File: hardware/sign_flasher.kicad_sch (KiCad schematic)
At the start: 39 parts, among them Q1 TBD, Q2 TBD, U1 NE555D, U2 NE555D

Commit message: finished design and layout with TODOs
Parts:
- added D12, D16, D20, D24, D4, D8: LED, LED_THT:LED_D5.0mm, symbol Device:LED
- added J1: Battery, Connector_JST:JST_XH_B2B-XH-A_1x02_P2.50mm_Vertical, symbol Connector:Conn_01x02_Socket
- C1: renamed from C3; value 10nF -> 10n; footprint (none) -> Capacitor_THT:CP_Radial_D4.0mm_P2.00mm
- C2: renamed from C5; value 2.2uF -> 2.2u; footprint (none) -> Capacitor_THT:CP_Radial_D4.0mm_P2.00mm; symbol Device:C -> Device:C_Polarized
- C3: renamed from C4; value 10nF -> 10n; footprint (none) -> Capacitor_THT:CP_Radial_D4.0mm_P2.00mm
- C4: renamed from C6; value 2.2uF -> 2.2u; footprint (none) -> Capacitor_THT:CP_Radial_D4.0mm_P2.00mm; symbol Device:C -> Device:C_Polarized
- C5: renamed from C1; value 220uF -> 220u
- D1, D2, D3: footprint (none) -> LED_THT:LED_D5.0mm
- D10: renamed from D8; footprint (none) -> LED_THT:LED_D5.0mm
- D11: renamed from D9; footprint (none) -> LED_THT:LED_D5.0mm
- D13: renamed from D10; footprint (none) -> LED_THT:LED_D5.0mm
- D14: renamed from D11; footprint (none) -> LED_THT:LED_D5.0mm
- D15: renamed from D12; footprint (none) -> LED_THT:LED_D5.0mm
- D17: renamed from D13; footprint (none) -> LED_THT:LED_D5.0mm
- D18: renamed from D14; footprint (none) -> LED_THT:LED_D5.0mm
- D19: renamed from D15; footprint (none) -> LED_THT:LED_D5.0mm
- D21: renamed from D16; footprint (none) -> LED_THT:LED_D5.0mm
- D22: renamed from D17; footprint (none) -> LED_THT:LED_D5.0mm
- D23: renamed from D18; footprint (none) -> LED_THT:LED_D5.0mm
- D5: renamed from D4; footprint (none) -> LED_THT:LED_D5.0mm
- D6: renamed from D5; footprint (none) -> LED_THT:LED_D5.0mm
- D7: renamed from D6; footprint (none) -> LED_THT:LED_D5.0mm
- D9: renamed from D7; footprint (none) -> LED_THT:LED_D5.0mm
- Q1: value TBD -> BC557; footprint (none) -> Package_TO_SOT_THT:TO-92; symbol Device:Q_PNP_BCE -> Device:Q_PNP_CBE
- Q2: value TBD -> BC547; footprint (none) -> Package_TO_SOT_THT:TO-92; symbol Device:Q_NPN_EBC -> Device:Q_NPN_CBE
- R1, R2, R3, R4, R7, R8: footprint (none) -> Resistor_THT:R_Axial_DIN0207_L6.3mm_D2.5mm_P7.62mm_Horizontal
- R5: renamed from R6; footprint (none) -> Resistor_THT:R_Axial_DIN0207_L6.3mm_D2.5mm_P7.62mm_Horizontal
- R6: renamed from R5; footprint (none) -> Resistor_THT:R_Axial_DIN0207_L6.3mm_D2.5mm_P7.62mm_Horizontal
- RV1: renamed from RV3; footprint (none) -> sign_flasher:TRIM_3306F-1-103
- RV2: renamed from RV1; footprint (none) -> sign_flasher:TRIM_3306F-1-103
- RV3: renamed from RV5; footprint (none) -> sign_flasher:TRIM_3306F-1-103
- RV4: footprint (none) -> sign_flasher:TRIM_3306F-1-103
- U1, U2: footprint Package_SO:SOIC-8_3.9x4.9mm_P1.27mm -> Package_DIP:DIP-8_W7.62mm
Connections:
- net 9V0: now also J1.1 (Pin_1)
- net GND: now also Q2.3 (E), D12.1 (K), D4.1 (K), D8.1 (K), J1.2 (Pin_2); no longer D11.1 (K), D3.1 (K), D7.1 (K), Q2.1 (E)
- net at R1.2: now also Q1.2 (B); no longer Q1.1 (B)
- net at R2.1, R3.1, R4.1: now also Q1.1 (C); no longer Q1.2 (C)
- new net: D7.1 (K), D8.2 (A)
- new net: D3.1 (K), D4.2 (A)
- new net: D16.1 (K), D20.1 (K), D24.1 (K), Q2.1 (C)
- new net: D23.1 (K), D24.2 (A)
- new net: D15.1 (K), D16.2 (A)
- new net: D19.1 (K), D20.2 (A)
- new net: D11.1 (K), D12.2 (A)
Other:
- moved on the sheet: Q2, R5

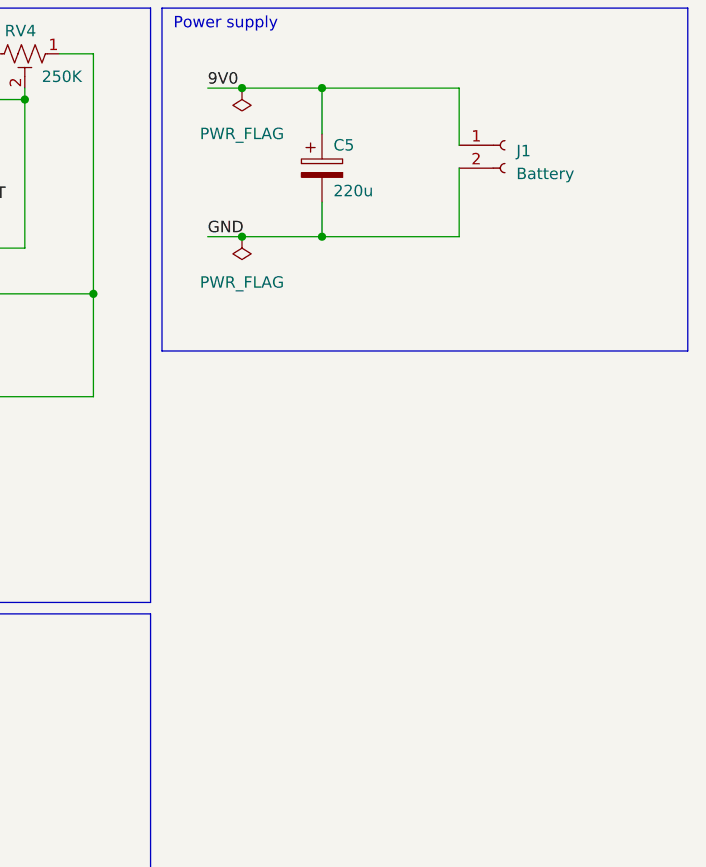
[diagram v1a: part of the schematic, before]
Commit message: get under 100mmsq, add mounting holes
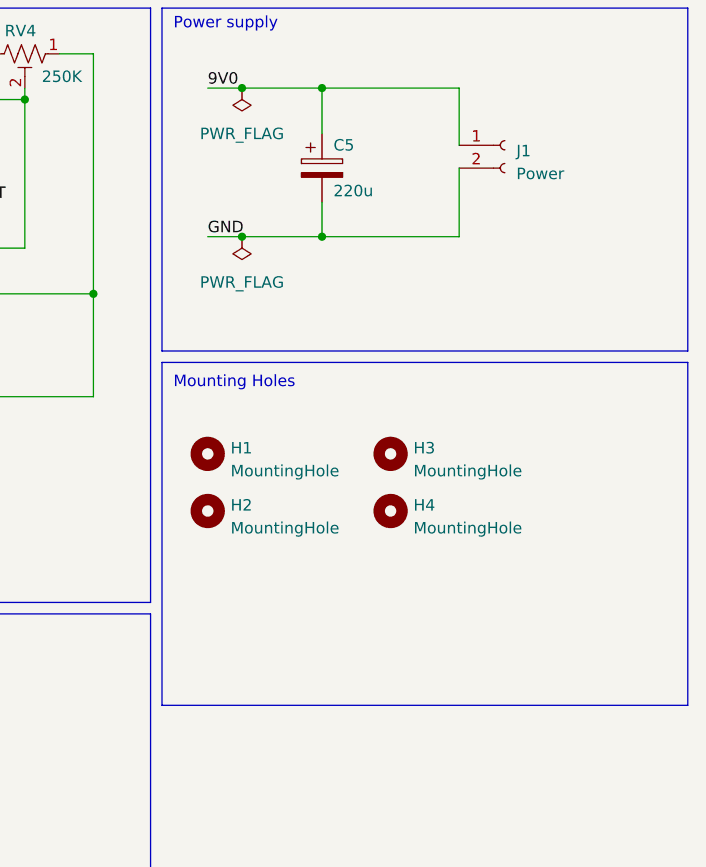
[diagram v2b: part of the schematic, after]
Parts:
- added H1, H2, H3, H4: MountingHole, MountingHole:MountingHole_4mm_Pad, symbol Mechanical:MountingHole
- J1: value Battery -> Power
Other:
- note added: "Mounting Holes"
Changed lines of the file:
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@@
+    (fill (type none))
+  )
+  (rectangle (start 144.78 52.07) (end 203.2 90.17)
+    (stroke (width 0) (type default))
     (fill (type none))
   )
@@
     (effects (font (size 1.27 1.27)) (justify left bottom))
   )
+  (text "Mounting Holes\n\n" (at 146.05 57.15 0)
+    (effects (font (size 1.27 1.27)) (justify left bottom))
+  )
   (text "Timing\n" (at 13.97 16.51 0)
     (effects (font (size 1.27 1.27)) (justify left bottom))
@@
         (path "/1d207b3d-09a4-4c99-885a-dd10de47bf46"
           (reference "#PWR04") (unit 1)
+        )
+      )
+    )
+  )
+  (symbol (lib_id "Mechanical:MountingHole") (at 170.18 62.23 0) (unit 1)
+    (in_bom yes) (on_board yes) (dnp no) (fields_autoplaced)
+    (property "Reference" "H3" (at 172.72 61.595 0)
+      (effects (font (size 1.27 1.27)) (justify left))
+    )
+    (property "Value" "MountingHole" (at 172.72 64.135 0)
+      (effects (font (size 1.27 1.27)) (justify left))
+    )
+    (property "Footprint" "MountingHole:MountingHole_4mm_Pad" (at 170.18 62.23 0)
+      (effects (font (size 1.27 1.27)) hide)
+    )
+    (property "Datasheet" "~" (at 170.18 62.23 0)
+      (effects (font (size 1.27 1.27)) hide)
+    )
+    (instances
+      (project "sign_flasher"
+        (path "/1d207b3d-09a4-4c99-885a-dd10de47bf46"
+          (reference "H3") (unit 1)
+        )
+      )
+    )
+  )
+  (symbol (lib_id "Mechanical:MountingHole") (at 149.86 62.23 0) (unit 1)
+    (in_bom yes) (on_board yes) (dnp no) (fields_autoplaced)
+    (property "Reference" "H1" (at 152.4 61.595 0)
+      (effects (font (size 1.27 1.27)) (justify left))
+    )
+    (property "Value" "MountingHole" (at 152.4 64.135 0)
+      (effects (font (size 1.27 1.27)) (justify left))
+    )
+    (property "Footprint" "MountingHole:MountingHole_4mm_Pad" (at 149.86 62.23 0)
+      (effects (font (size 1.27 1.27)) hide)
+    )
+    (property "Datasheet" "~" (at 149.86 62.23 0)
+      (effects (font (size 1.27 1.27)) hide)
+    )
+    (instances
+      (project "sign_flasher"
+        (path "/1d207b3d-09a4-4c99-885a-dd10de47bf46"
+          (reference "H1") (unit 1)
         )
       )
@@
     )
   )
+  (symbol (lib_id "Mechanical:MountingHole") (at 149.86 68.58 0) (unit 1)
+    (in_bom yes) (on_board yes) (dnp no) (fields_autoplaced)
+    (property "Reference" "H2" (at 152.4 67.945 0)
+      (effects (font (size 1.27 1.27)) (justify left))
+    )
+    (property "Value" "MountingHole" (at 152.4 70.485 0)
+      (effects (font (size 1.27 1.27)) (justify left))
+    )
+    (property "Footprint" "MountingHole:MountingHole_4mm_Pad" (at 149.86 68.58 0)
+      (effects (font (size 1.27 1.27)) hide)
+    )
+    (property "Datasheet" "~" (at 149.86 68.58 0)
+      (effects (font (size 1.27 1.27)) hide)
+    )
+    (instances
+      (project "sign_flasher"
+        (path "/1d207b3d-09a4-4c99-885a-dd10de47bf46"
+          (reference "H2") (unit 1)
+        )
+      )
+    )
+  )
   (symbol (lib_id "Timer:NE555D") (at 44.45 39.37 0) (unit 1)
     (in_bom yes) (on_board yes) (dnp no) (fields_autoplaced)
@@
     )
   )
+  (symbol (lib_id "Mechanical:MountingHole") (at 170.18 68.58 0) (unit 1)
+    (in_bom yes) (on_board yes) (dnp no) (fields_autoplaced)
+    (property "Reference" "H4" (at 172.72 67.945 0)
+      (effects (font (size 1.27 1.27)) (justify left))
+    )
+    (property "Value" "MountingHole" (at 172.72 70.485 0)
+      (effects (font (size 1.27 1.27)) (justify left))
+    )
+    (property "Footprint" "MountingHole:MountingHole_4mm_Pad" (at 170.18 68.58 0)
+      (effects (font (size 1.27 1.27)) hide)
+    )
+    (property "Datasheet" "~" (at 170.18 68.58 0)
+      (effects (font (size 1.27 1.27)) hide)
+    )
+    (instances
+      (project "sign_flasher"
+        (path "/1d207b3d-09a4-4c99-885a-dd10de47bf46"
+          (reference "H4") (unit 1)
+        )
+      )
+    )
+  )
   (symbol (lib_id "power:GND") (at 24.13 50.8 0) (unit 1)
     (in_bom yes) (on_board yes) (dnp no) (fields_autoplaced)
@@
       (effects (font (size 1.27 1.27)) (justify left))
     )
-    (property "Value" "Battery" (at 184.15 31.115 0)
-      (effects (font (size 1.27 1.27)) (justify left))
-    )
+    (property "Value" "Power" (at 184.15 31.115 0)
+      (effects (font (size 1.27 1.27)) (justify left))
+    )

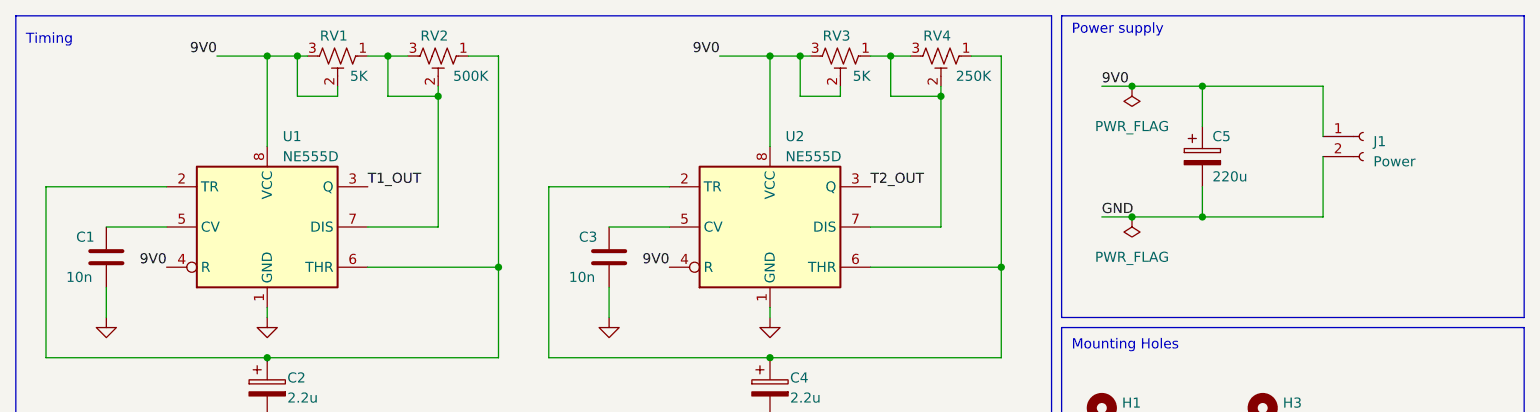
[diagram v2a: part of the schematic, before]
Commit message: Address issues identified with rev v0.01:
 - Revise schematic to indicate the need for 12V power
 - Add reverse voltage protection diode
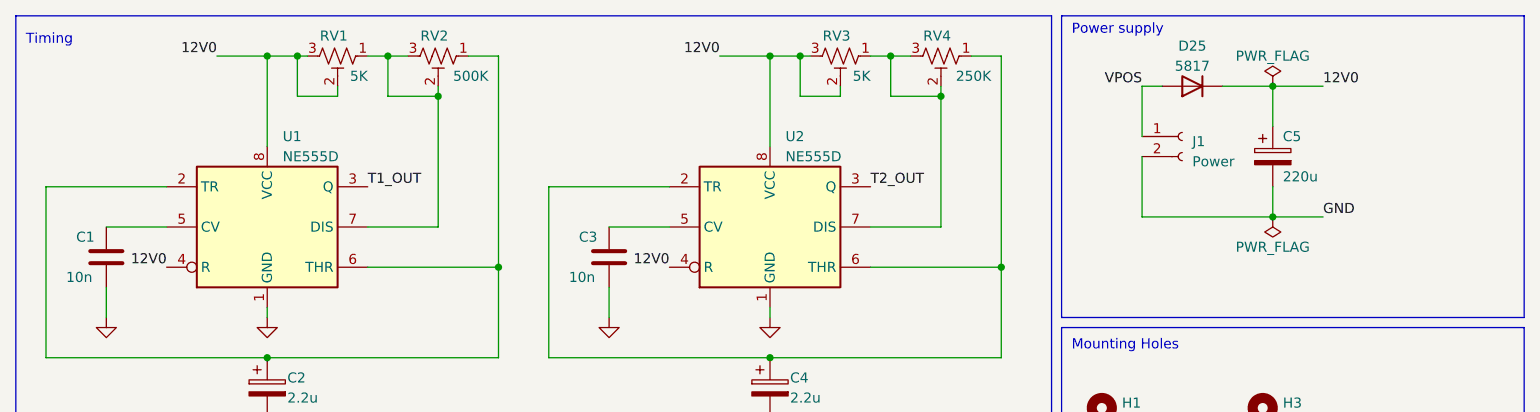
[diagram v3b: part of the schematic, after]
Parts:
- added D25: 5817, Diode_THT:D_DO-41_SOD81_P7.62mm_Horizontal, symbol Device:D
- C1, C3: footprint Capacitor_THT:CP_Radial_D4.0mm_P2.00mm -> Capacitor_THT:C_Rect_L7.2mm_W2.5mm_P5.00mm_FKS2_FKP2_MKS2_MKP2
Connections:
- net 9V0 renamed 12V0
- net 12V0: now also D25.1 (K); no longer J1.1 (Pin_1)
- new net VPOS: D25.2 (A), J1.1 (Pin_1)
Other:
- moved on the sheet: C5
